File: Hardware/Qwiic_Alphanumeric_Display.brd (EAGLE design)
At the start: 40.6 x 27.9 mm, 45 parts, among them J4 Vertical Qwiic Connector, J5 Vertical Qwiic Connector, U2 XC9140

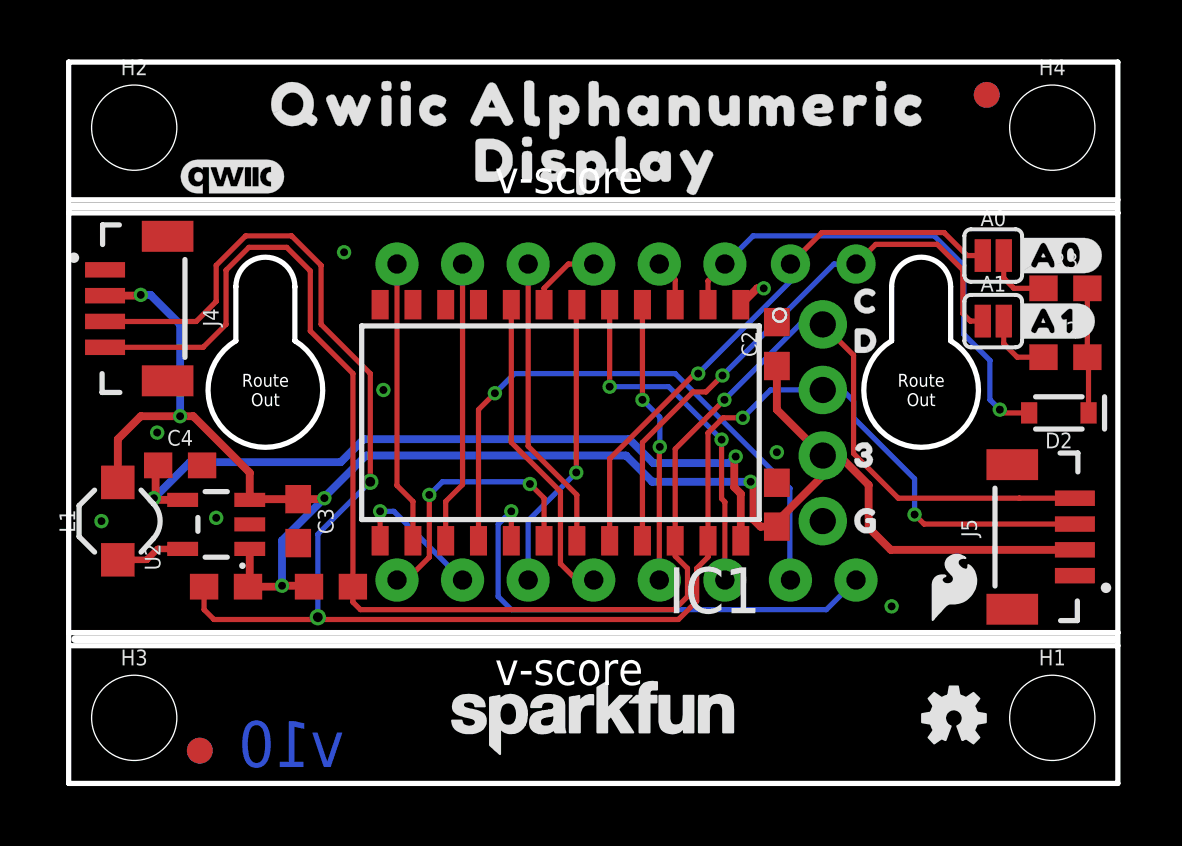
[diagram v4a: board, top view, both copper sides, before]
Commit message: Updates from Review:
* Mirrored J3 on sch
* Updated via size so that they're all the same
* Added GND vias near qwiic connectors
* Flipped C1, re-routed
* Moved SDA trace so that copper would flow in dead space (bottom)
* Added I2C jumper and changed pull up resistors to 0402, 1K
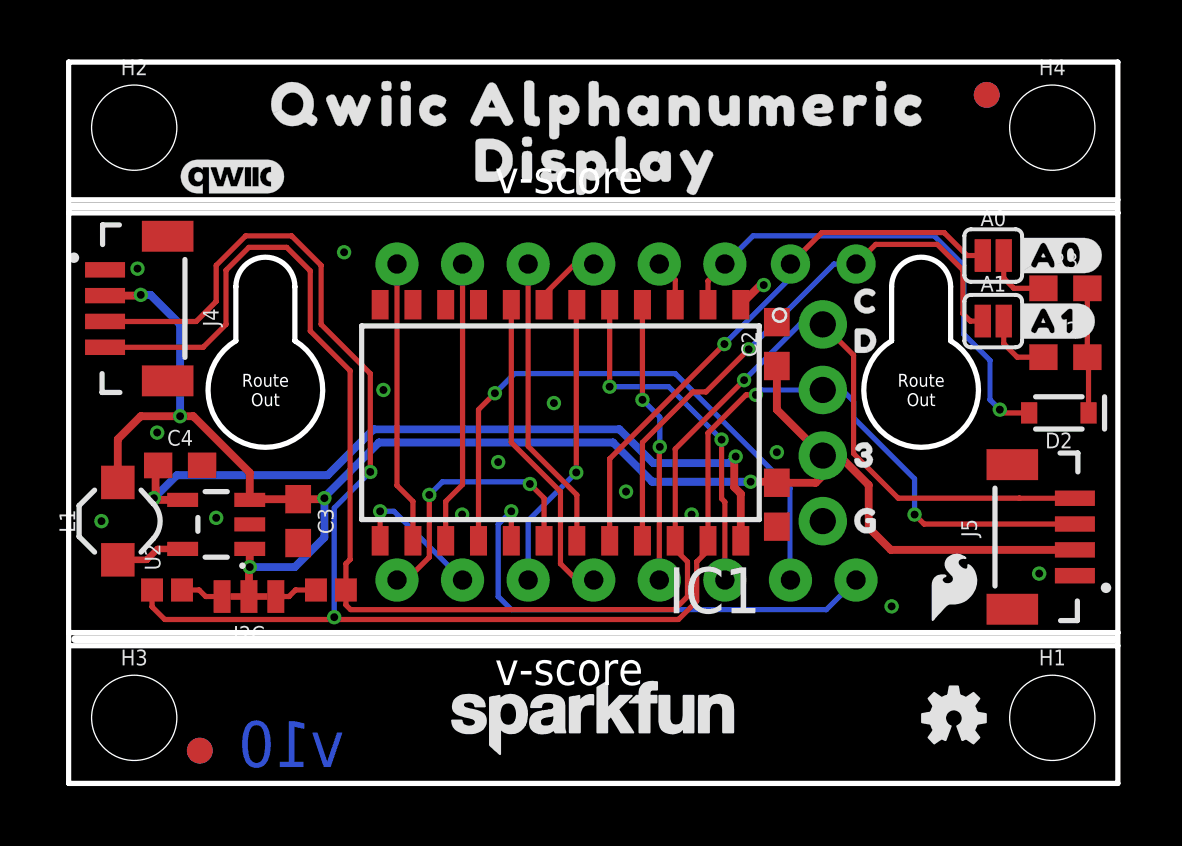
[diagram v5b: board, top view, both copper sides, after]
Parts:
- added I2C: JUMPER-SMT_3_2-NC_TRACE_NO-SILK, SparkFun-Jumpers:SMT-JUMPER_3_2-NC_TRACE_NO-SILK
- R4, R5: value 4.7k -> 1KOHM-0402-1/16W-1%; device SparkFun-Resistors:0603 -> SparkFun-Resistors:0402
- moved R4 2.29 mm to (3.81, 7.49)
- moved R5 0.13 mm to (10.2, 7.49)
- turned C1 to 270 degrees
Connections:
- new net N$1: I2C.3, R4.2
- new net N$4: I2C.1, R5.2
- net 3.3V: now also I2C.2; no longer R4.2, R5.2
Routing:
- net 3.3V: track 67.1 -> 63.9 mm
- net N$1: track 0.00 -> 1.66 mm
- net N$4: track 0.00 -> 1.66 mm
- net SDA: track 71.7 -> 73.3 mm
- net GND: track 1.15 -> 1.20 mm, vias 8 -> 15
